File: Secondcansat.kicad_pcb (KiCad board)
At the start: 2 copper layers, 74 x 74 mm, 66 parts, among them IC1 XBP9B-XCWT-001, J1 OpenlogBreakout, J10 SDA, J11 5V, J12 Tx, J13 Rx, J14 Battery_Holder_keystone 1079, J2 Camera, J3 Pressure_MS5607, J4 Debugger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

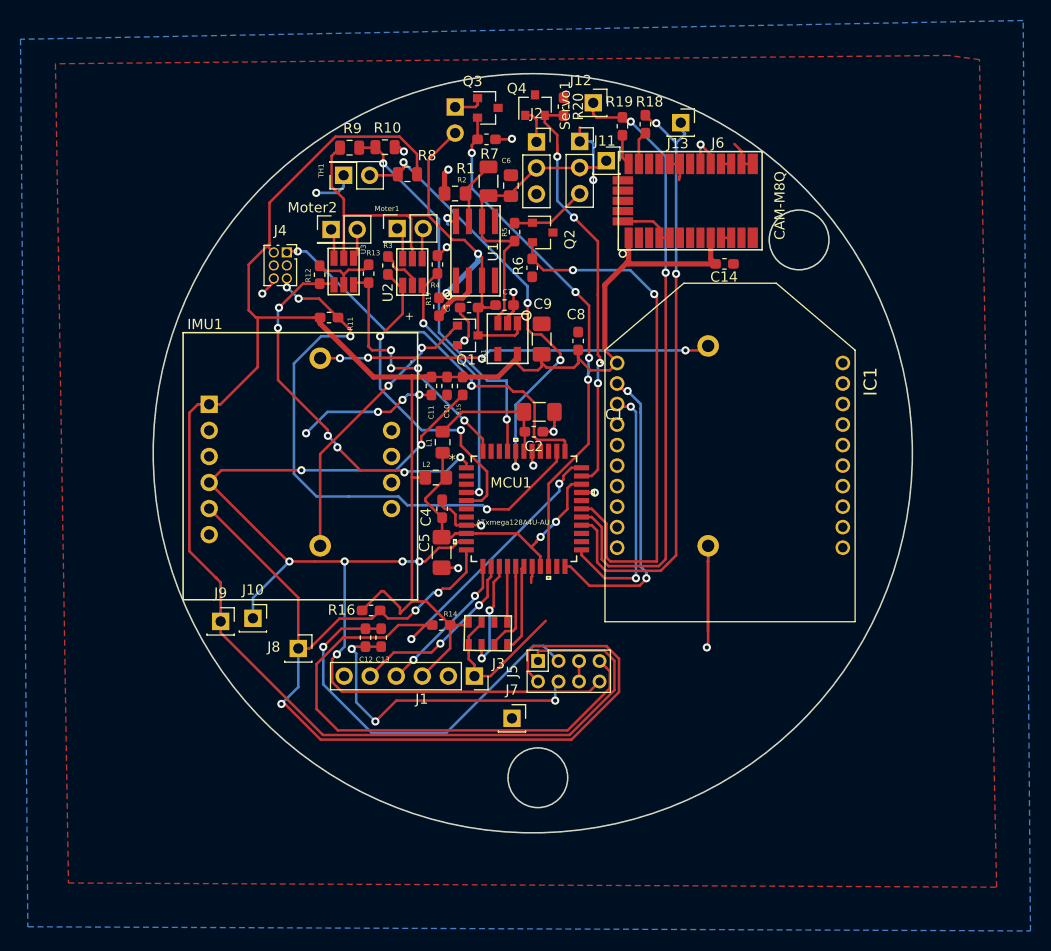
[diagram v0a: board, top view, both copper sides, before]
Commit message: added backup power and usb mini connector
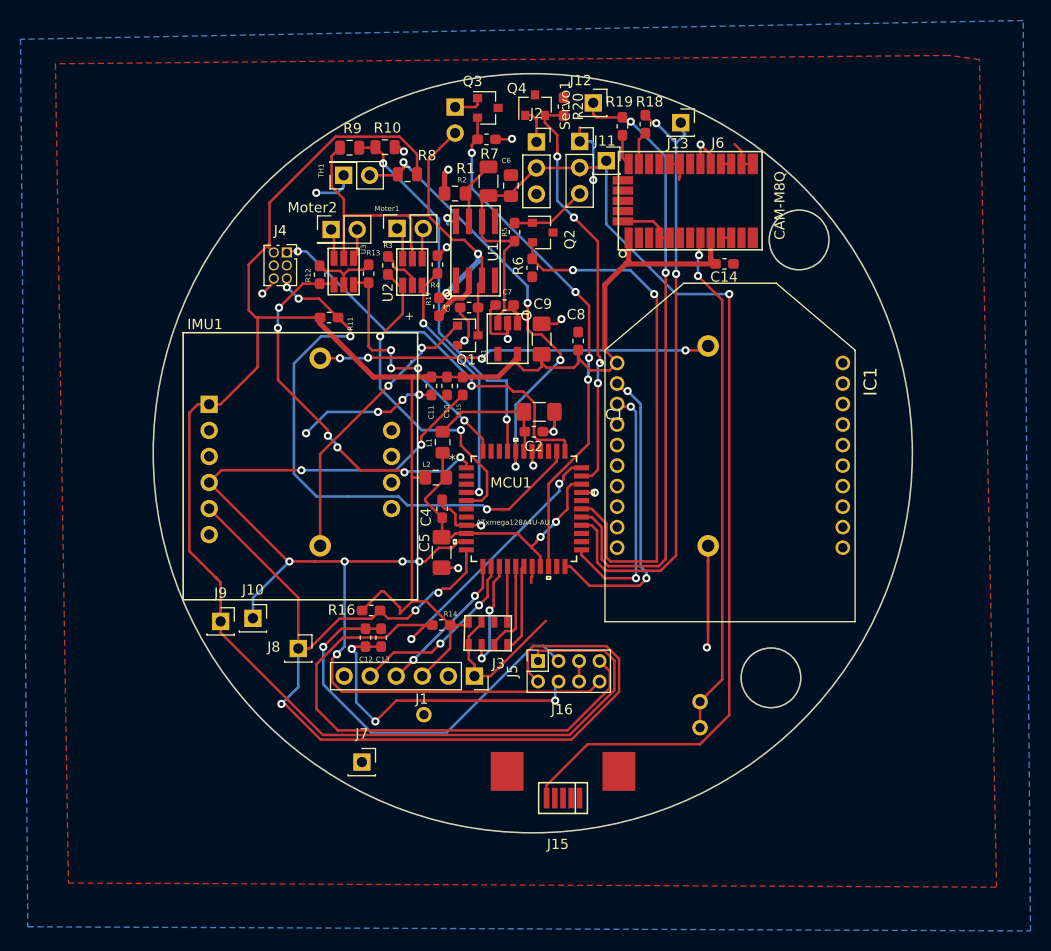
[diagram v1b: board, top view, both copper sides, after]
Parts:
- added J15: USB_B_Mini, CanSAT2ndtry:USB-Mini, F.Cu at (89.6, 132.3)
- added J16: coinBattery, CanSAT2ndtry:coin_Battery_120591-1, F.Cu at (89.5, 124.2)
- moved J7 15.2 mm to (70.0, 128.8)
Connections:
- C7 pad 1: GND -> +5V
- C7 pad 2: +6V -> GND
- VR1 pad 1: +6V -> +5V
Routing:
- net +5V: track 30.2 -> 118.0 mm, vias 0 -> 1
- net Net-(J16-Pad2): track 0.00 -> 49.7 mm, vias 0 -> 2
- net +6V: track 60.7 -> 54.1 mm
- net GND: track 118.9 -> 125.5 mm, vias 21 -> 22
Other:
- outline, holes or cut-outs redrawn

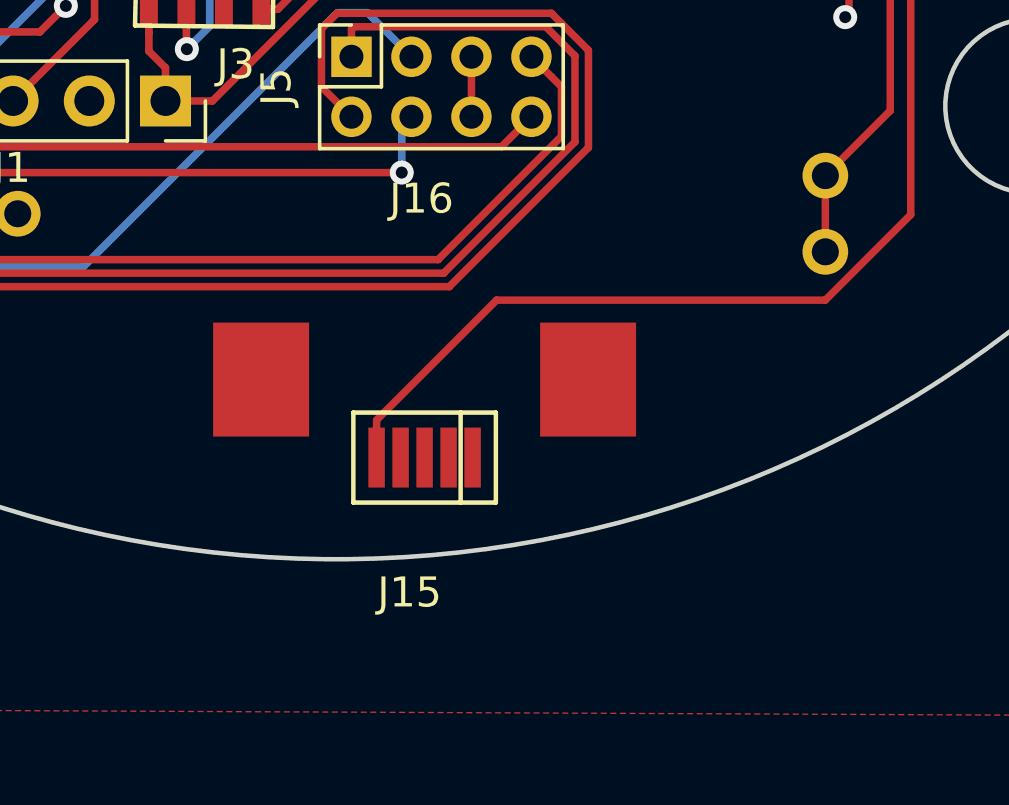
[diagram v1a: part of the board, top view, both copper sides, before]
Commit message: Flipped MicroUSB
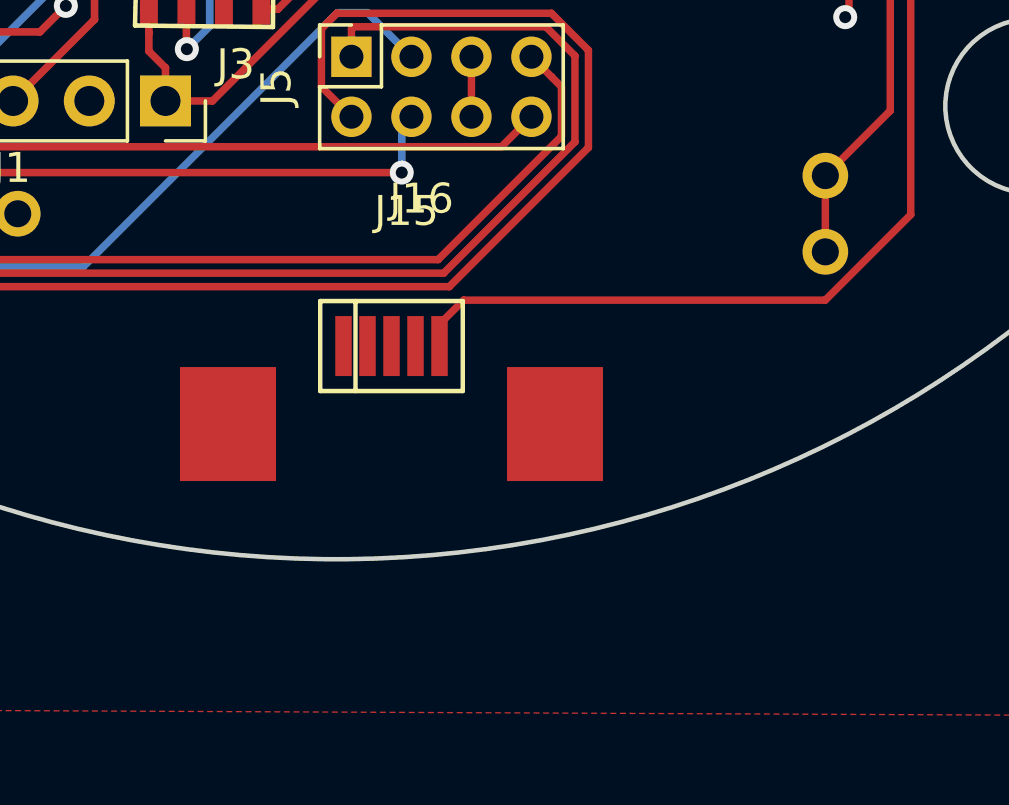
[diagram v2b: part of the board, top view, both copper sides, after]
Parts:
- moved J15 3.88 mm to (88.5, 128.6), turned to 0 degrees
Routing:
- net +5V: track 118.0 -> 114.0 mm
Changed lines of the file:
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@@
   )
   (module CanSAT2ndtry:USB-Mini (layer F.Cu)
-    (at 89.5604 132.2832 180)
-    (fp_text reference J15 (at 0.5 -4.5 180) (layer F.SilkS)
+    (at 88.4572 128.5656)
+    (fp_text reference J15 (at 0.5 -4.5) (layer F.SilkS)
       (effects (font (size 1 1) (thickness 0.15)))
     )
-    (fp_text value USB_B_Mini (at 0 -2.5 180) (layer F.Fab)
+    (fp_text value USB_B_Mini (at 0 -2.5) (layer F.Fab)
       (effects (font (size 1 1) (thickness 0.15)))
     )
@@
     (fp_line (start 2.55 1.65) (end -2.55 1.65) (layer F.CrtYd) (width 0.05))
     (fp_line (start -2.55 1.65) (end -2.55 -1.65) (layer F.CrtYd) (width 0.05))
-    (pad 5 smd rect (at -1.6 0 180) (size 0.55 2) (layers F.Cu F.Paste F.Mask)
+    (pad 5 smd rect (at -1.6 0) (size 0.55 2) (layers F.Cu F.Paste F.Mask)
       (net 1 GND))
-    (pad 4 smd rect (at -0.8 0 180) (size 0.55 2) (layers F.Cu F.Paste F.Mask)
+    (pad 4 smd rect (at -0.8 0) (size 0.55 2) (layers F.Cu F.Paste F.Mask)
       (net 97 "Net-(J15-Pad4)"))
-    (pad 3 smd rect (at 0 0 180) (size 0.55 2) (layers F.Cu F.Paste F.Mask)
+    (pad 3 smd rect (at 0 0) (size 0.55 2) (layers F.Cu F.Paste F.Mask)
       (net 98 "Net-(J15-Pad3)"))
-    (pad 2 smd rect (at 0.8 0 180) (size 0.55 2) (layers F.Cu F.Paste F.Mask)
+    (pad 2 smd rect (at 0.8 0) (size 0.55 2) (layers F.Cu F.Paste F.Mask)
       (net 99 "Net-(J15-Pad2)"))
-    (pad 1 smd rect (at 1.6 0 180) (size 0.55 2) (layers F.Cu F.Paste F.Mask)
+    (pad 1 smd rect (at 1.6 0) (size 0.55 2) (layers F.Cu F.Paste F.Mask)
       (net 6 +5V))
-    (pad 7 smd rect (at 5.45 2.6 180) (size 3.2 3.8) (layers F.Cu F.Paste F.Mask))
-    (pad 6 smd rect (at -5.45 2.6 180) (size 3.2 3.8) (layers F.Cu F.Paste F.Mask)
+    (pad 7 smd rect (at 5.45 2.6) (size 3.2 3.8) (layers F.Cu F.Paste F.Mask))
+    (pad 6 smd rect (at -5.45 2.6) (size 3.2 3.8) (layers F.Cu F.Paste F.Mask)
       (net 100 "Net-(J15-Pad6)"))
   )
@@
   (segment (start 105.7656 124.187162) (end 105.7656 83.1596) (width 0.25) (layer F.Cu) (net 6))
   (segment (start 102.91693 127.035832) (end 105.7656 124.187162) (width 0.25) (layer F.Cu) (net 6))
-  (segment (start 91.957768 127.035832) (end 102.91693 127.035832) (width 0.25) (layer F.Cu) (net 6))
-  (segment (start 87.9604 132.2832) (end 87.9604 131.0332) (width 0.25) (layer F.Cu) (net 6))
-  (segment (start 87.9604 131.0332) (end 91.957768 127.035832) (width 0.25) (layer F.Cu) (net 6))
   (segment (start 93.7768 71.2548) (end 93.7768 70.1548) (width 0.25) (layer B.Cu) (net 6))
   (segment (start 93.7768 76.349002) (end 93.7768 71.2548) (width 0.25) (layer B.Cu) (net 6))
@@
   (segment (start 85.1104 85.0516) (end 84.75653 84.69773) (width 0.25) (layer F.Cu) (net 6))
   (segment (start 85.1104 86.0016) (end 85.1104 85.0516) (width 0.25) (layer F.Cu) (net 6))
+  (segment (start 90.861968 127.035832) (end 102.91693 127.035832) (width 0.25) (layer F.Cu) (net 6))
+  (segment (start 90.0572 127.8406) (end 90.861968 127.035832) (width 0.25) (layer F.Cu) (net 6))
+  (segment (start 90.0572 128.5656) (end 90.0572 127.8406) (width 0.25) (layer F.Cu) (net 6))
   (segment (start 60.946399 78.245601) (end 60.946399 74.252051) (width 0.25) (layer F.Cu) (net 7))
   (segment (start 75.3318 69.51405) (end 75.3318 70.6756) (width 0.25) (layer F.Cu) (net 7))
